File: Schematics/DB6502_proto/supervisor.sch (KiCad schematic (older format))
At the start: 29 parts, among them SW1 Reset, U10 FT230XS, U11 74HC595, U12 74HC157, U13 ATmega644PA-PU, U14 74AC74, U15 DS1813, U16 74AC74, U17 74AC08, U8 74AC04, X1 8MHz, Y1 20MHz

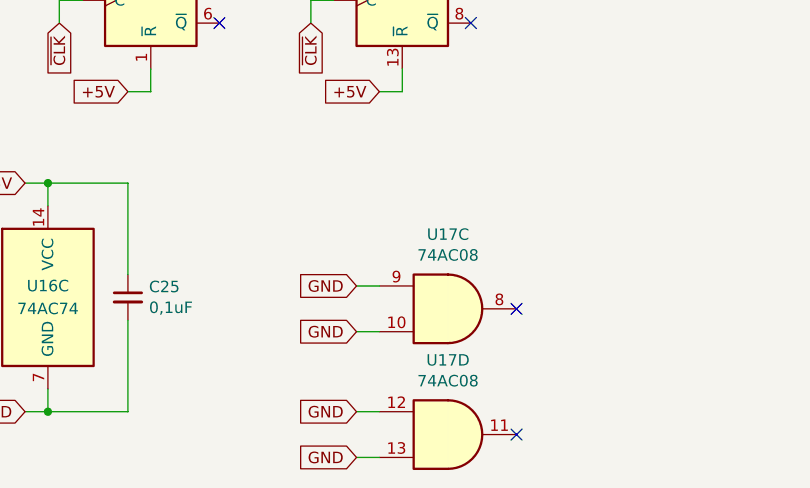
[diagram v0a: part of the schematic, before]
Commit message: Added latch feature for EXRAM
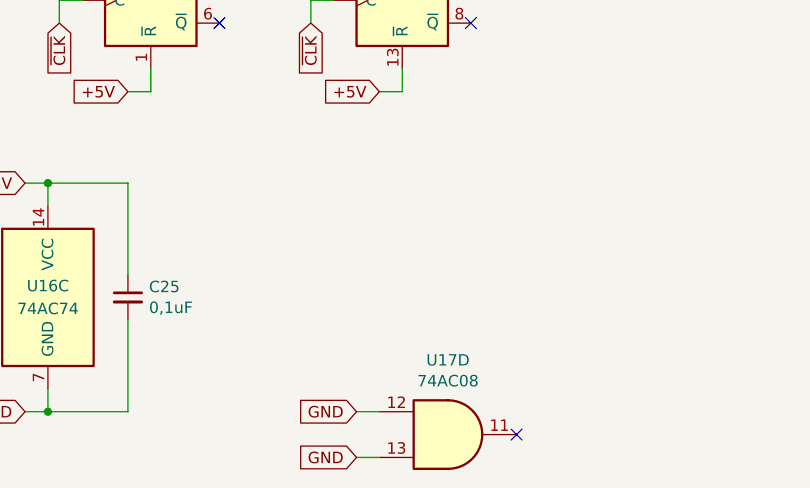
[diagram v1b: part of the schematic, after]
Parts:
- removed unit 3 of U17
- R11, R12: footprint Resistor_THT:R_Axial_DIN0207_L6.3mm_D2.5mm_P10.16mm_Horizontal -> Resistor_SMD:R_1206_3216Metric_Pad1.42x1.75mm_HandSolder
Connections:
- no-connect marks 13 -> 12
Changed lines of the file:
@@
 F 0 "R11" V 9850 2150 50  0000 C CNN
 F 1 "470" V 9750 2150 50  0000 C CNN
-F 2 "Resistor_THT:R_Axial_DIN0207_L6.3mm_D2.5mm_P10.16mm_Horizontal" V 9680 2150 50  0001 C CNN
+F 2 "Resistor_SMD:R_1206_3216Metric_Pad1.42x1.75mm_HandSolder" V 9680 2150 50  0001 C CNN
 F 3 "~" H 9750 2150 50  0001 C CNN
 	1    9750 2150
@@
 F 0 "R12" V 9850 2450 50  0000 C CNN
 F 1 "470" V 9750 2450 50  0000 C CNN
-F 2 "Resistor_THT:R_Axial_DIN0207_L6.3mm_D2.5mm_P10.16mm_Horizontal" V 9680 2450 50  0001 C CNN
+F 2 "Resistor_SMD:R_1206_3216Metric_Pad1.42x1.75mm_HandSolder" V 9680 2450 50  0001 C CNN
 F 3 "~" H 9750 2450 50  0001 C CNN
 	1    9750 2450
@@
 Wire Wire Line
 	2200 5000 2300 5000
-$Comp
-L 74xx:74LS08 U17
-U 3 1 5FA8DB46
-P 5550 6750
-AR Path="/5F8F4E1E/5FA8DB46" Ref="U17"  Part="3"
-AR Path="/5FA8DB46" Ref="U?"  Part="2"
-F 0 "U17" H 5550 7075 50  0000 C CNN
-F 1 "74AC08" H 5550 6984 50  0000 C CNN
-F 2 "Package_SO:SOIC-14_3.9x8.7mm_P1.27mm" H 5550 6750 50  0001 C CNN
-F 3 "https://www.ti.com/lit/ds/symlink/sn74ac08.pdf" H 5550 6750 50  0001 C CNN
-	3    5550 6750
-	1    0    0    -1
-$EndComp
-Text GLabel 5150 6650 0    50   Input ~ 0
-GND
-Text GLabel 5150 6850 0    50   Input ~ 0
-GND
-Wire Wire Line
-	5150 6850 5250 6850
-Wire Wire Line
-	5150 6650 5250 6650
-NoConn ~ 5850 6750
 Text GLabel 6100 1100 1    50   Output ~ 0
 WS_DISABLE

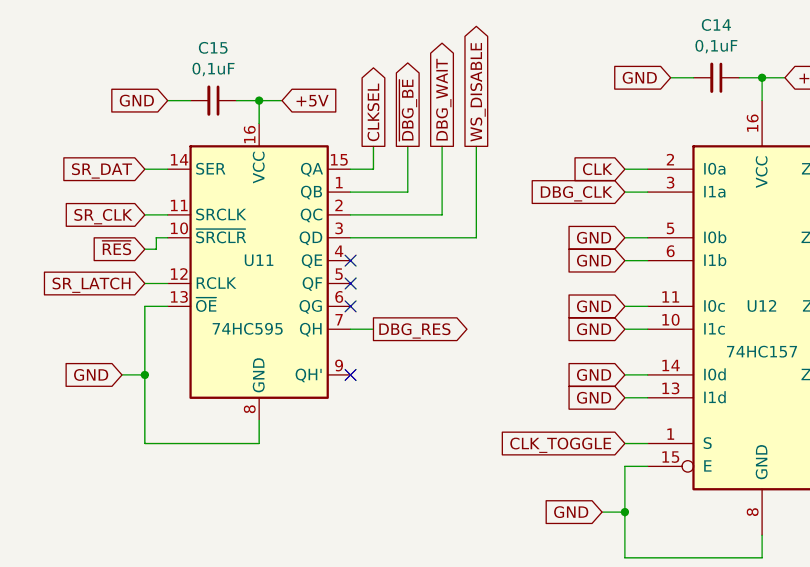
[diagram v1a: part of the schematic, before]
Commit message: Added bus labels
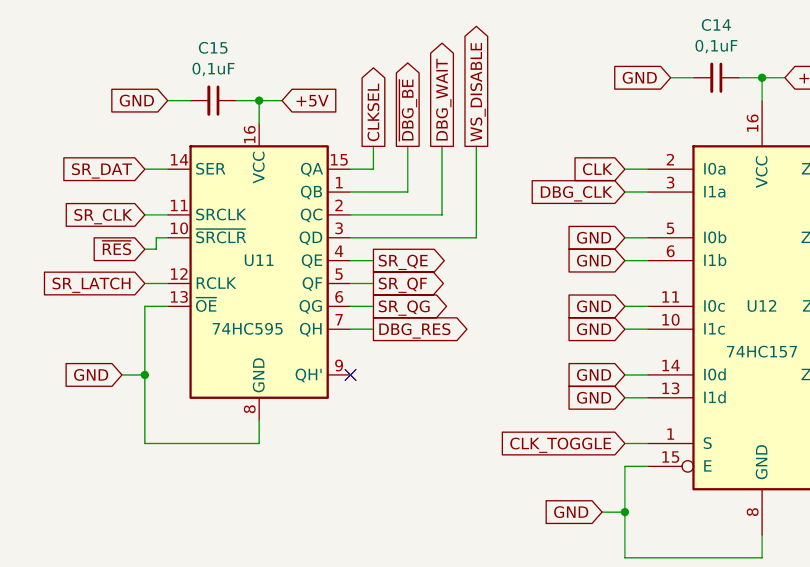
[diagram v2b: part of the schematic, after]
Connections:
- net SR_QE: now reaches U11.4 (QE)
- net SR_QF: now reaches U11.5 (QF)
- net SR_QG: now reaches U11.6 (QG)
- no-connect marks 12 -> 9
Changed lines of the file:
@@
 Wire Wire Line
 	6750 1500 6850 1500
-NoConn ~ 5550 1600
-NoConn ~ 5550 1700
-NoConn ~ 5550 1800
 Wire Wire Line
 	5650 1200 5650 1100
@@
 Wire Wire Line
 	9650 5500 9850 5500
+Text GLabel 5650 1600 2    50   Output ~ 0
+SR_QE
+Text GLabel 5650 1700 2    50   Output ~ 0
+SR_QF
+Text GLabel 5650 1800 2    50   Output ~ 0
+SR_QG
+Wire Wire Line
+	5550 1800 5650 1800
+Wire Wire Line
+	5550 1700 5650 1700
+Wire Wire Line
+	5550 1600 5650 1600
 Wire Bus Line
 	3200 2200 3200 2900

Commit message: Added one last line to the system
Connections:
- net BE: now also U17.11; no longer U8.4
- net GND: no longer U17.12, U17.13
- new net: U17.12, U8.4
- new net EXT_BE: U17.13
- no-connect marks 9 -> 8
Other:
- moved on the sheet: U17D, U8B
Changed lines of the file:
@@
 L 74xx:74LS04 U8
 U 2 1 5F92D3FA
-P 8300 5600
-F 0 "U8" H 8300 5917 50  0000 C CNN
-F 1 "74AC04" H 8300 5826 50  0000 C CNN
-F 2 "Package_SO:SOIC-14_3.9x8.7mm_P1.27mm" H 8300 5600 50  0001 C CNN
-F 3 "https://www.ti.com/lit/ds/symlink/sn74ac04.pdf" H 8300 5600 50  0001 C CNN
-	2    8300 5600
-	1    0    0    -1
-$EndComp
-Text GLabel 7900 5600 0    50   Input ~ 0
+P 5550 6600
+F 0 "U8" H 5550 6917 50  0000 C CNN
+F 1 "74AC04" H 5550 6826 50  0000 C CNN
+F 2 "Package_SO:SOIC-14_3.9x8.7mm_P1.27mm" H 5550 6600 50  0001 C CNN
+F 3 "https://www.ti.com/lit/ds/symlink/sn74ac04.pdf" H 5550 6600 50  0001 C CNN
+	2    5550 6600
+	1    0    0    -1
+$EndComp
+Text GLabel 5150 6600 0    50   Input ~ 0
 ~DBG_BE
 Wire Wire Line
-	7900 5600 8000 5600
-Text GLabel 8700 5600 2    50   Output ~ 0
+	5150 6600 5250 6600
+Text GLabel 6650 6700 2    50   Output ~ 0
 BE
 Wire Wire Line
-	8600 5600 8700 5600
+	5850 6600 5950 6600
 $Comp
 L 74xx:74LS04 U8
@@
 L 74xx:74LS08 U17
 U 4 1 5FBB5F74
-P 5550 7300
-F 0 "U17" H 5550 7625 50  0000 C CNN
-F 1 "74AC08" H 5550 7534 50  0000 C CNN
-F 2 "Package_SO:SOIC-14_3.9x8.7mm_P1.27mm" H 5550 7300 50  0001 C CNN
-F 3 "https://www.ti.com/lit/ds/symlink/sn74ac08.pdf" H 5550 7300 50  0001 C CNN
-	4    5550 7300
-	1    0    0    -1
-$EndComp
-Text GLabel 5150 7400 0    50   Input ~ 0
-GND
-Text GLabel 5150 7200 0    50   Input ~ 0
-GND
-Wire Wire Line
-	5150 7400 5250 7400
-Wire Wire Line
-	5150 7200 5250 7200
-NoConn ~ 5850 7300
+P 6250 6700
+F 0 "U17" H 6250 7025 50  0000 C CNN
+F 1 "74AC08" H 6250 6934 50  0000 C CNN
+F 2 "Package_SO:SOIC-14_3.9x8.7mm_P1.27mm" H 6250 6700 50  0001 C CNN
+F 3 "https://www.ti.com/lit/ds/symlink/sn74ac08.pdf" H 6250 6700 50  0001 C CNN
+	4    6250 6700
+	1    0    0    -1
+$EndComp
 Wire Wire Line
 	9750 5700 9850 5700
@@
 Wire Wire Line
 	5550 1600 5650 1600
+Wire Wire Line
+	6550 6700 6650 6700
+Text GLabel 5850 6800 0    50   Input ~ 0
+EXT_BE
+Wire Wire Line
+	5850 6800 5950 6800
 Wire Bus Line
 	3200 2200 3200 2900

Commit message: PCB RC2
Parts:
- C17, C18: footprint Capacitor_THT:C_Disc_D5.0mm_W2.5mm_P2.50mm -> Capacitor_SMD:C_1206_3216Metric_Pad1.33x1.80mm_HandSolder
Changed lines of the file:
@@
 F 0 "C17" V 1279 1400 50  0000 C CNN
 F 1 "22pF" V 1188 1400 50  0000 C CNN
-F 2 "Capacitor_THT:C_Disc_D5.0mm_W2.5mm_P2.50mm" H 1050 1400 50  0001 C CNN
+F 2 "Capacitor_SMD:C_1206_3216Metric_Pad1.33x1.80mm_HandSolder" H 1050 1400 50  0001 C CNN
 F 3 "~" H 1050 1400 50  0001 C CNN
 	1    1050 1400
@@
 F 0 "C18" V 900 1600 50  0000 C CNN
 F 1 "22pF" V 800 1600 50  0000 C CNN
-F 2 "Capacitor_THT:C_Disc_D5.0mm_W2.5mm_P2.50mm" H 1050 1600 50  0001 C CNN
+F 2 "Capacitor_SMD:C_1206_3216Metric_Pad1.33x1.80mm_HandSolder" H 1050 1600 50  0001 C CNN
 F 3 "~" H 1050 1600 50  0001 C CNN
 	1    1050 1600

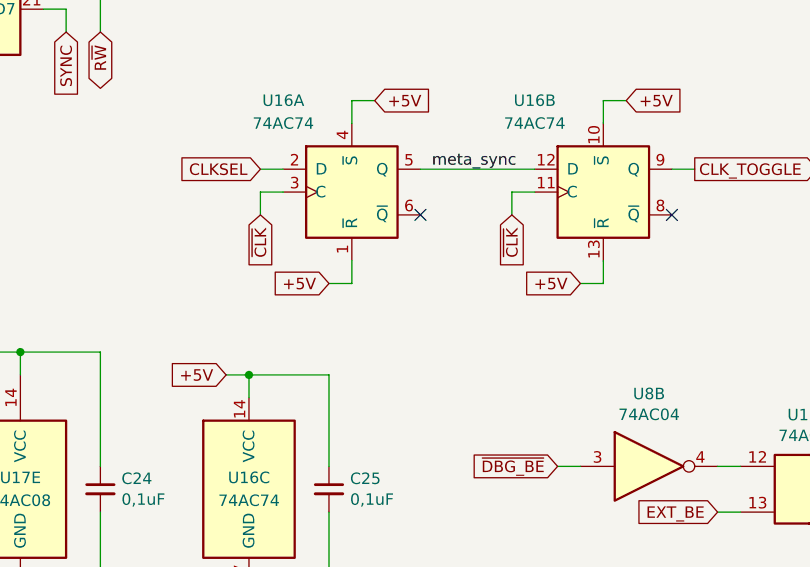
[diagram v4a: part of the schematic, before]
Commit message: Last minute updates (remove VCC from AVRISP)
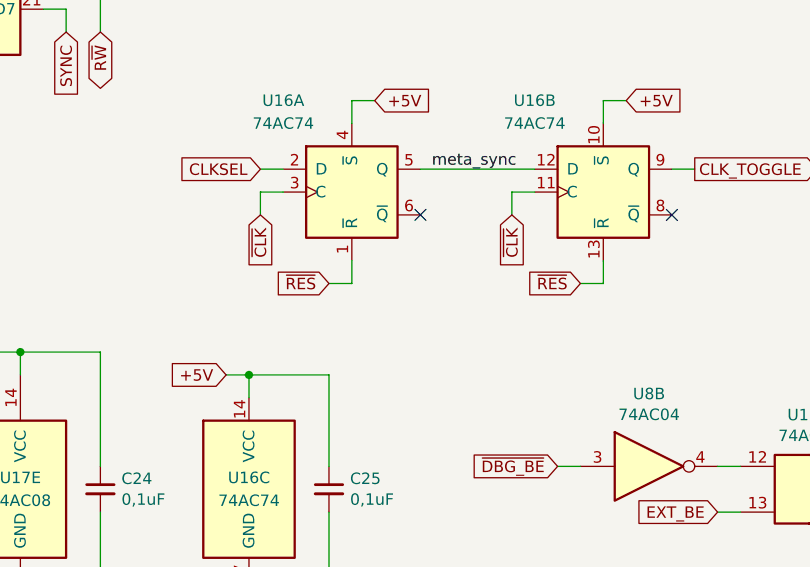
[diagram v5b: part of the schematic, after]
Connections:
- net +5V: no longer U16.1 (~R), U16.13 (~R)
- net ~RES: now also U16.1 (~R), U16.13 (~R)
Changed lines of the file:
@@
 Wire Wire Line
 	5250 5800 5350 5800
-Text GLabel 5250 5800 0    50   Input ~ 0
-+5V
 Wire Wire Line
 	4250 5000 4350 5000
@@
 Wire Wire Line
 	4250 5800 4250 5700
-Text GLabel 4150 5800 0    50   Input ~ 0
-+5V
 Text GLabel 4350 5000 2    50   Input ~ 0
 +5V
@@
 Wire Bus Line
 	3950 1300 3950 3900
+Text GLabel 4150 5800 0    50   Input ~ 0
+~RES
+Text GLabel 5250 5800 0    50   Input ~ 0
+~RES
 $EndSCHEMATC

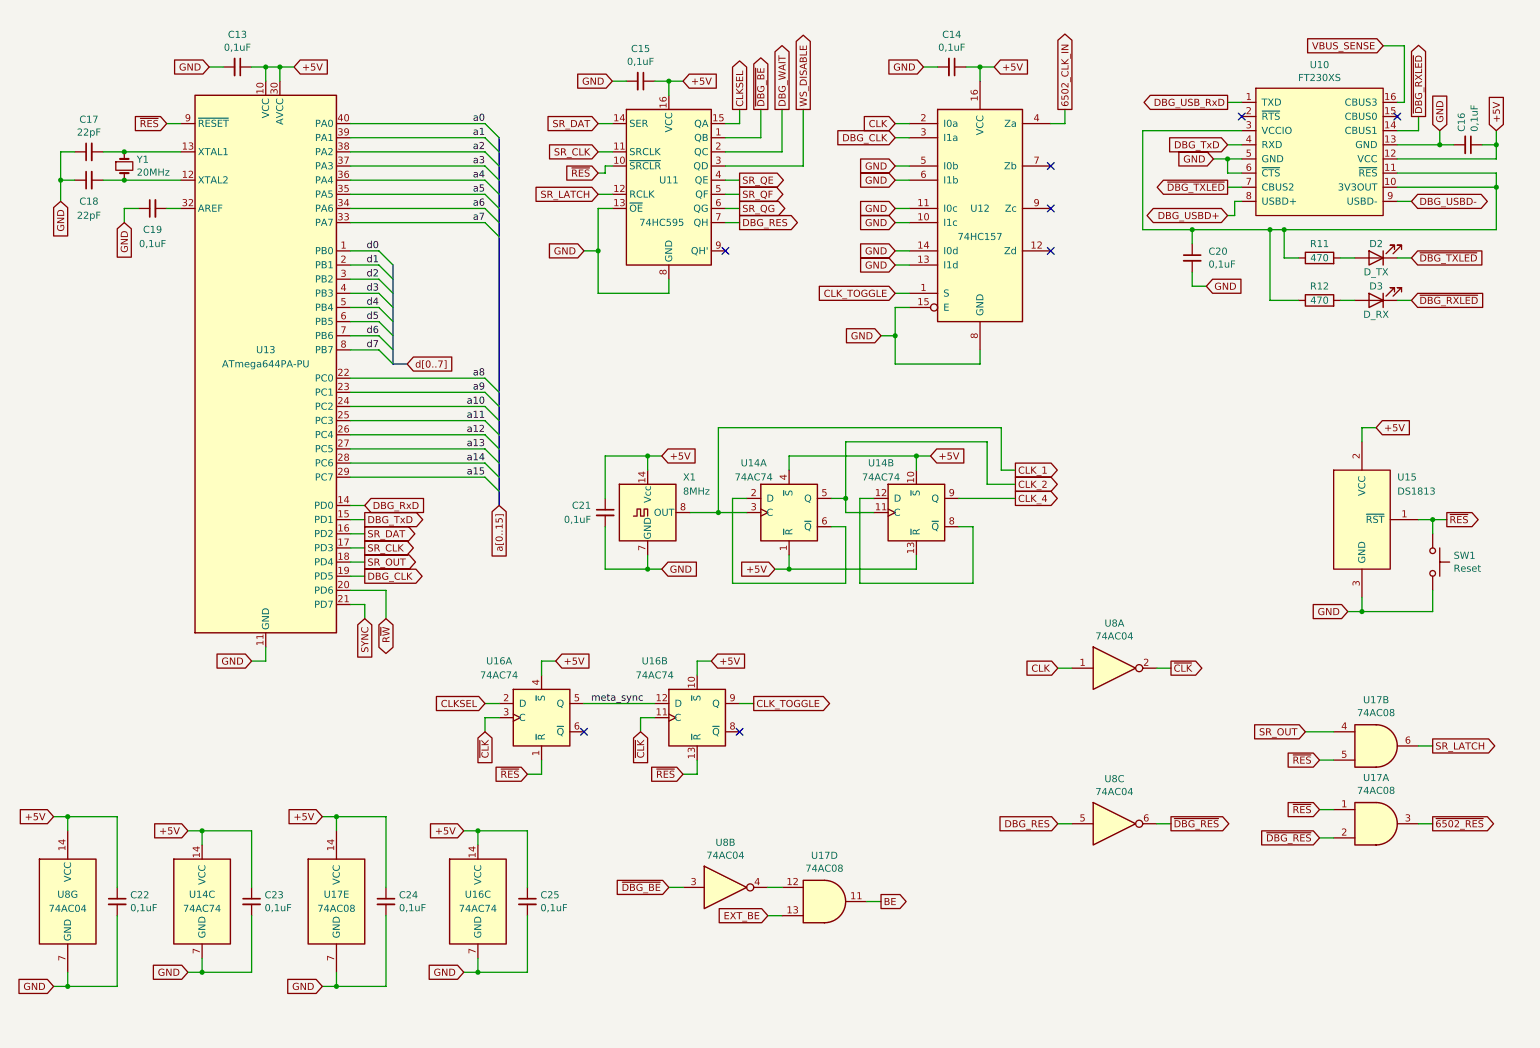
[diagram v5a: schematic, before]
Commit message: Working on massively redesigned board
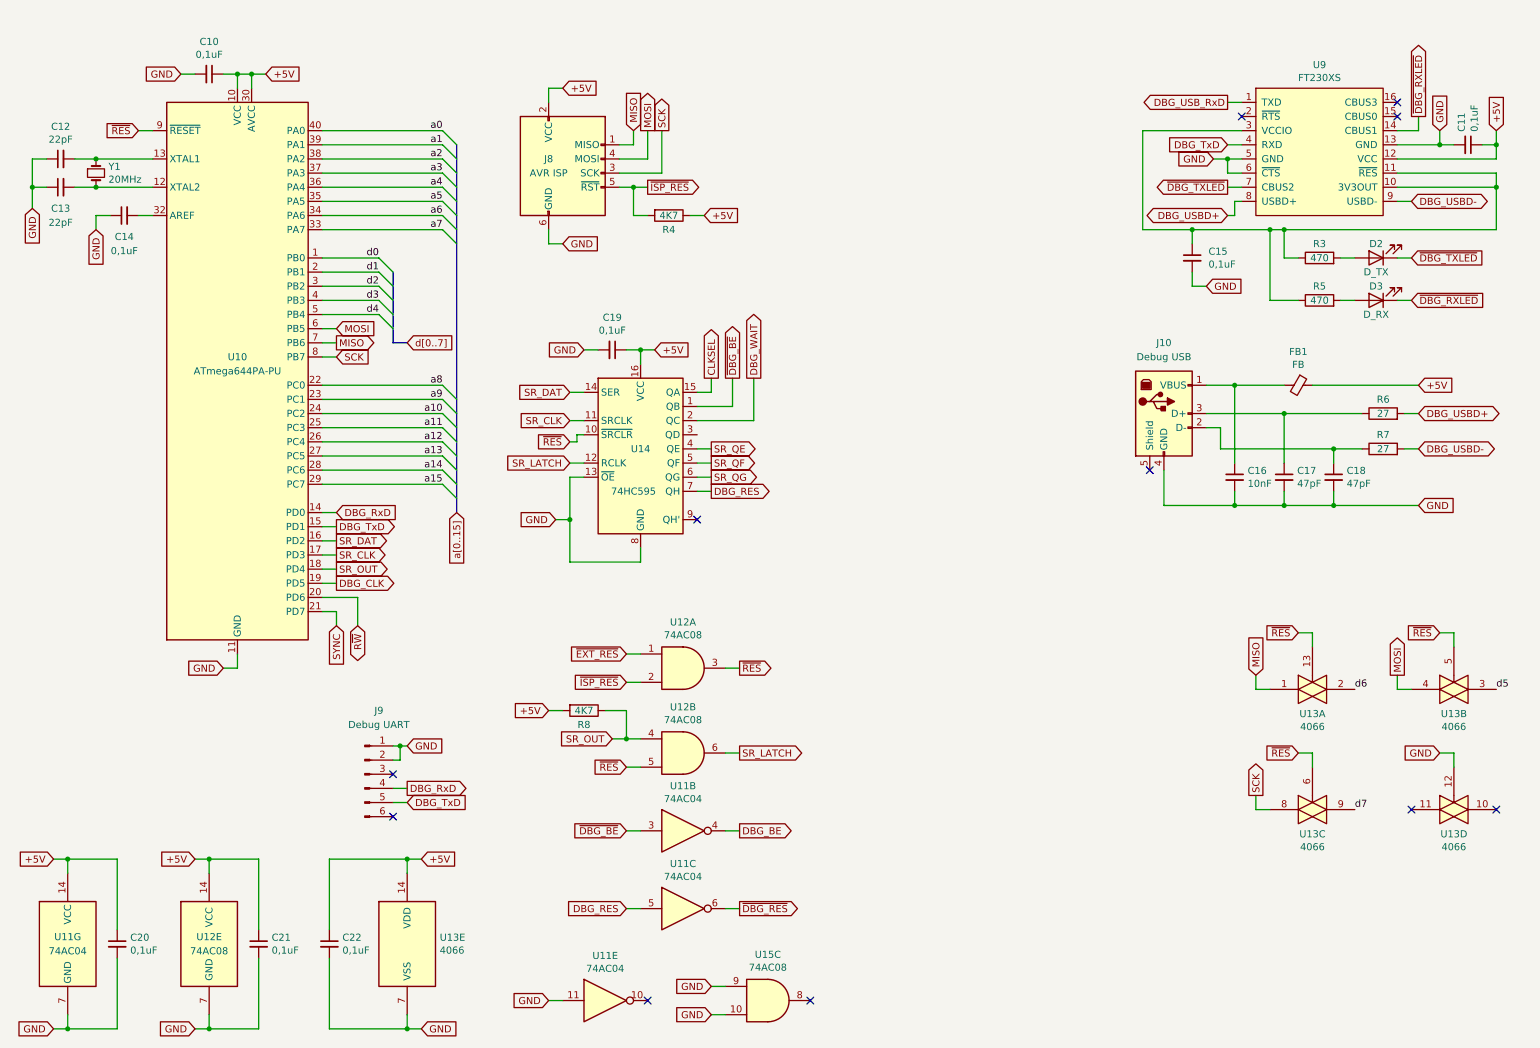
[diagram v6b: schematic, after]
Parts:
- removed C14, C21, C23, C25: 0,1uF, Capacitor_SMD:C_1206_3216Metric_Pad1.42x1.75mm_HandSolder, symbol Device:C_Small
- removed SW1: Reset, Button_Switch_THT:SW_PUSH_6mm_H4.3mm, symbol Switch:SW_Push
- removed U12: 74HC157, Package_SO:SOIC-16_3.9x9.9mm_P1.27mm, symbol 74xx:74LS157
- removed U14, U16: 74AC74, Package_SO:SOIC-14_3.9x8.7mm_P1.27mm, symbol 74xx:74HC74
- removed U15: DS1813, Package_TO_SOT_THT:TO-92_Inline_Wide, symbol 6502:DS1813
- removed unit 1 of U17
- removed unit 4 of U17
- removed unit 1 of U8
- removed X1: 8MHz, Oscillator:Oscillator_DIP-14, symbol Oscillator:ACO-xxxMHz
- added C16: 10nF, Capacitor_SMD:C_1206_3216Metric_Pad1.33x1.80mm_HandSolder, symbol Device:C_Small
- added C17, C18: 47pF, Capacitor_SMD:C_1206_3216Metric_Pad1.33x1.80mm_HandSolder, symbol Device:C_Small
- added C22: 0,1uF, Capacitor_SMD:C_1206_3216Metric_Pad1.33x1.80mm_HandSolder, symbol Device:C_Small
- added FB1: FB, Resistor_SMD:R_1206_3216Metric_Pad1.30x1.75mm_HandSolder, symbol Device:Ferrite_Bead_Small
- added J10: Debug USB, Connector_USB:USB_B_OST_USB-B1HSxx_Horizontal, symbol 6502:USB_B
- added J8: AVR ISP, Connector_PinHeader_2.54mm:PinHeader_2x03_P2.54mm_Vertical, symbol Connector:AVR-ISP-6
- added J9: Debug UART, Connector_PinHeader_2.54mm:PinHeader_1x06_P2.54mm_Horizontal, symbol Connector:Conn_01x06_Male
- added R4, R8: 4K7, Resistor_SMD:R_1206_3216Metric_Pad1.30x1.75mm_HandSolder, symbol Device:R
- added R6, R7: 27, Resistor_SMD:R_1206_3216Metric_Pad1.30x1.75mm_HandSolder, symbol Device:R
- added unit 5 of U11
- added unit 1 of U12
- added U13: 4066, Package_SO:SOIC-14_3.9x8.7mm_P1.27mm, symbol 4xxx:4066
- added U15: 74AC08, Package_SO:SOIC-14_3.9x8.7mm_P1.27mm, symbol 74xx:74LS08
- C10: renamed from C13; footprint Capacitor_SMD:C_1206_3216Metric_Pad1.42x1.75mm_HandSolder -> Capacitor_SMD:C_1206_3216Metric_Pad1.33x1.80mm_HandSolder
- C11: renamed from C16; footprint Capacitor_SMD:C_1206_3216Metric_Pad1.42x1.75mm_HandSolder -> Capacitor_SMD:C_1206_3216Metric_Pad1.33x1.80mm_HandSolder
- C14: renamed from C19; footprint Capacitor_SMD:C_1206_3216Metric_Pad1.42x1.75mm_HandSolder -> Capacitor_SMD:C_1206_3216Metric_Pad1.33x1.80mm_HandSolder
- C15: renamed from C20; footprint Capacitor_SMD:C_1206_3216Metric_Pad1.42x1.75mm_HandSolder -> Capacitor_SMD:C_1206_3216Metric_Pad1.33x1.80mm_HandSolder
- C19: renamed from C15; footprint Capacitor_SMD:C_1206_3216Metric_Pad1.42x1.75mm_HandSolder -> Capacitor_SMD:C_1206_3216Metric_Pad1.33x1.80mm_HandSolder
- C20: renamed from C22; footprint Capacitor_SMD:C_1206_3216Metric_Pad1.42x1.75mm_HandSolder -> Capacitor_SMD:C_1206_3216Metric_Pad1.33x1.80mm_HandSolder
- C21: renamed from C24; footprint Capacitor_SMD:C_1206_3216Metric_Pad1.42x1.75mm_HandSolder -> Capacitor_SMD:C_1206_3216Metric_Pad1.33x1.80mm_HandSolder
- R3: renamed from R11; footprint Resistor_SMD:R_1206_3216Metric_Pad1.42x1.75mm_HandSolder -> Resistor_SMD:R_1206_3216Metric_Pad1.30x1.75mm_HandSolder
- R5: renamed from R12; footprint Resistor_SMD:R_1206_3216Metric_Pad1.42x1.75mm_HandSolder -> Resistor_SMD:R_1206_3216Metric_Pad1.30x1.75mm_HandSolder
- U9: renamed from U10; footprint Package_SO:SSOP-16_5.3x6.2mm_P0.65mm -> Package_SO:SSOP-16_4.4x5.2mm_P0.65mm
- renumbered C17 to C12, C18 to C13, U13 to U10, U8 to U11, U17 to U12, U11 to U14
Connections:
- net +5V: now also C22.1, FB1.1, J8.2 (VCC), R4.1, R8.2, U13.14 (VDD)
- net DBG_RxD: now also J9.4 (Pin_4)
- net DBG_TxD: now also J9.5 (Pin_5)
- net DBG_USBD+: now also R6.2
- net DBG_USBD-: now also R7.2
- net GND: now also C16.2, C17.2, C18.2, C22.2, J10.4 (GND), J8.6 (GND), J9.1 (Pin_1), J9.2 (Pin_2), U11.11, U13.12, U13.7 (VSS), U15.10, U15.9
- net SR_OUT: now also R8.1
- net d5: now also U13.3; no longer U10.6 (PB5)
- net d6: now also U13.2; no longer U10.7 (PB6)
- net d7: now also U13.9; no longer U10.8 (PB7)
- net ~RES: now also U12.3, U13.13, U13.5, U13.6
- net DBG_BE: now reaches U11.4
- net VBUS_SENSE: no longer names the net of U9.16 (CBUS3)
- net WS_DISABLE: no longer names the net of U14.3 (QD)
- new net: C16.1, FB1.2, J10.1 (VBUS)
- new net: C18.1, J10.2 (D-), R7.1
- new net: C17.1, J10.3 (D+), R6.1
- new net MISO: J8.1 (MISO), U10.7 (PB6), U13.1
- new net MOSI: J8.4 (MOSI), U10.6 (PB5), U13.4
- new net SCK: J8.3 (SCK), U10.8 (PB7), U13.8
- new net ~EXT_RES: U12.1
- new net ~ISP_RES: J8.5 (~RST), R4.2, U12.2
- no-connect marks 8 -> 11
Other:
- moved on the sheet: C10, C12, C13, C14, C19, C20, C21, U10, U11B, U11C, U11G, U12B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
